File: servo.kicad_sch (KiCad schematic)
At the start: 13 parts, among them J301 pow, M301 Motor_Servo, Q301 BC547, SW301 switch, SW302 switch, U301 LM555xN

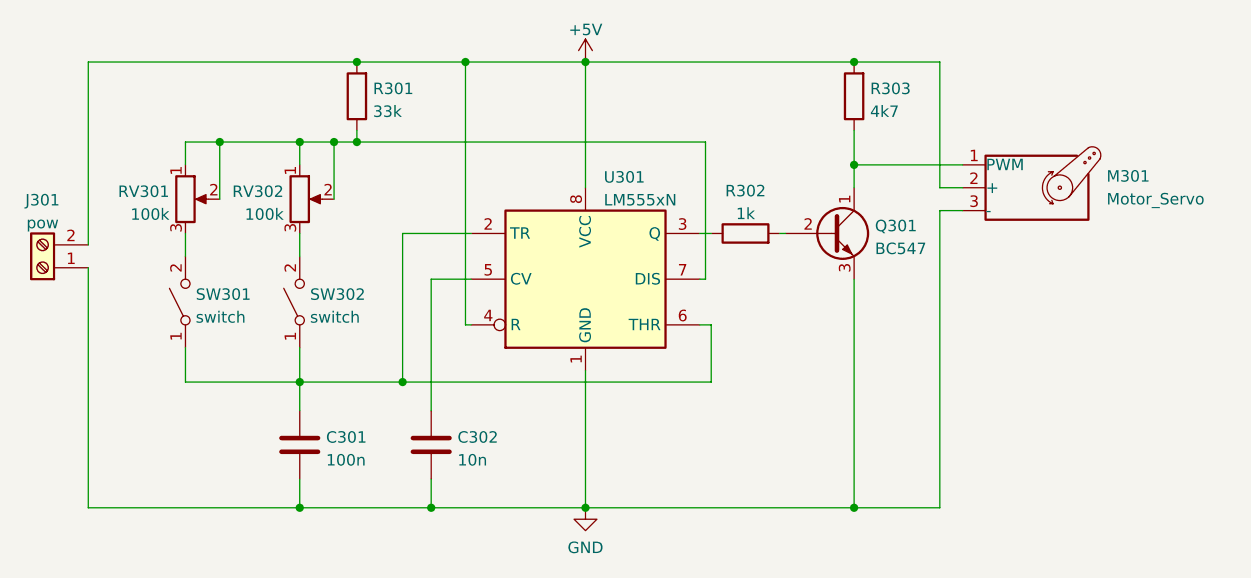
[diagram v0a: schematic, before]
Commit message: added hierarchial labels to some schematics
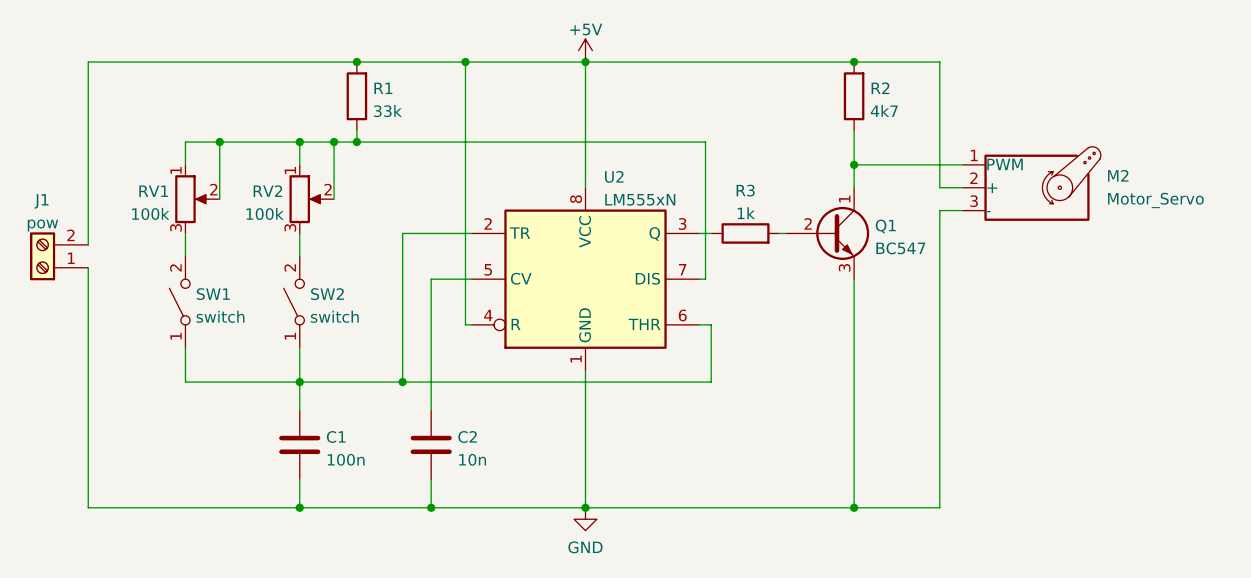
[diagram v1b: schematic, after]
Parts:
- renumbered C301 to C1, C302 to C2, J301 to J1, M301 to M2, Q301 to Q1, R301 to R1, R303 to R2, R302 to R3, RV301 to RV1, RV302 to RV2, SW301 to SW1, SW302 to SW2, U301 to U2

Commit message: moved some schematic scheets to their own folders and routed a board with it. This allow for re-use of PCB parts.
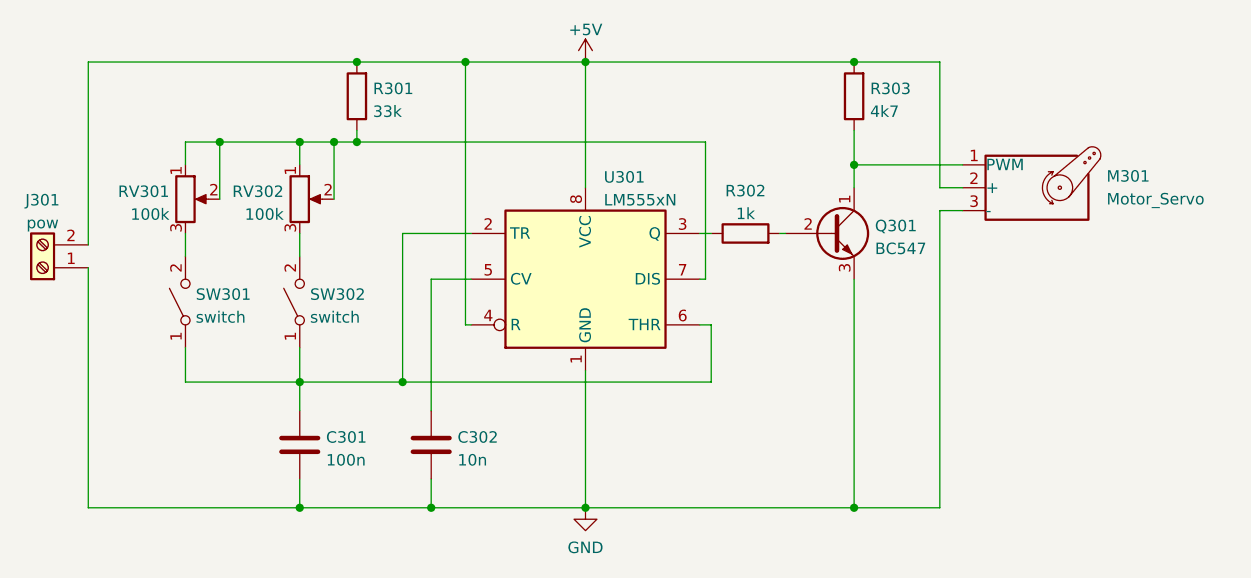
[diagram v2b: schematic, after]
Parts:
- renumbered C1 to C301, C2 to C302, J1 to J301, M2 to M301, Q1 to Q301, R1 to R301, R3 to R302, R2 to R303, RV1 to RV301, RV2 to RV302, SW1 to SW301, SW2 to SW302, U2 to U301
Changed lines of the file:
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@@
   (symbol (lib_id "Device:R_Potentiometer") (at 127 78.74 0) (unit 1)
     (in_bom yes) (on_board yes) (dnp no) (fields_autoplaced)
-    (property "Reference" "RV2" (at 125.2221 77.9053 0)
+    (property "Reference" "RV302" (at 125.2221 77.9053 0)
       (effects (font (size 1.27 1.27)) (justify right))
     )
@@
       (project "general_schematics"
         (path "/e777d9ec-d073-4229-a9e6-2cf85636e407/c8788370-a7f5-4096-b7be-5f9bdb412f73"
-          (reference "RV2") (unit 1)
+          (reference "RV302") (unit 1)
         )
       )
@@
   (symbol (lib_id "Device:R") (at 176.53 82.55 90) (unit 1)
     (in_bom yes) (on_board yes) (dnp no) (fields_autoplaced)
-    (property "Reference" "R3" (at 176.53 77.8342 90)
+    (property "Reference" "R302" (at 176.53 77.8342 90)
       (effects (font (size 1.27 1.27)))
     )
@@
       (project "general_schematics"
         (path "/e777d9ec-d073-4229-a9e6-2cf85636e407/c8788370-a7f5-4096-b7be-5f9bdb412f73"
-          (reference "R3") (unit 1)
+          (reference "R302") (unit 1)
         )
       )
@@
   (symbol (lib_id "Device:C") (at 141.605 106.045 0) (unit 1)
     (in_bom yes) (on_board yes) (dnp no) (fields_autoplaced)
-    (property "Reference" "C2" (at 144.526 105.2103 0)
+    (property "Reference" "C302" (at 144.526 105.2103 0)
       (effects (font (size 1.27 1.27)) (justify left))
     )
@@
       (project "general_schematics"
         (path "/e777d9ec-d073-4229-a9e6-2cf85636e407/c8788370-a7f5-4096-b7be-5f9bdb412f73"
-          (reference "C2") (unit 1)
+          (reference "C302") (unit 1)
         )
       )
@@
   (symbol (lib_id "Device:C") (at 127 106.045 0) (unit 1)
     (in_bom yes) (on_board yes) (dnp no) (fields_autoplaced)
-    (property "Reference" "C1" (at 129.921 105.2103 0)
+    (property "Reference" "C301" (at 129.921 105.2103 0)
       (effects (font (size 1.27 1.27)) (justify left))
     )
@@
       (project "general_schematics"
         (path "/e777d9ec-d073-4229-a9e6-2cf85636e407/c8788370-a7f5-4096-b7be-5f9bdb412f73"
-          (reference "C1") (unit 1)
+          (reference "C301") (unit 1)
         )
       )
@@
   (symbol (lib_id "power:GND") (at 158.75 113.03 0) (unit 1)
     (in_bom yes) (on_board yes) (dnp no) (fields_autoplaced)
-    (property "Reference" "#PWR04" (at 158.75 119.38 0)
+    (property "Reference" "#PWR0103" (at 158.75 119.38 0)
       (effects (font (size 1.27 1.27)) hide)
     )
@@
       (project "general_schematics"
         (path "/e777d9ec-d073-4229-a9e6-2cf85636e407/c8788370-a7f5-4096-b7be-5f9bdb412f73"
-          (reference "#PWR04") (unit 1)
+          (reference "#PWR0103") (unit 1)
         )
       )
@@
   (symbol (lib_id "Device:R_Potentiometer") (at 114.3 78.74 0) (unit 1)
     (in_bom yes) (on_board yes) (dnp no) (fields_autoplaced)
-    (property "Reference" "RV1" (at 112.5221 77.9053 0)
+    (property "Reference" "RV301" (at 112.5221 77.9053 0)
       (effects (font (size 1.27 1.27)) (justify right))
     )
@@
       (project "general_schematics"
         (path "/e777d9ec-d073-4229-a9e6-2cf85636e407/c8788370-a7f5-4096-b7be-5f9bdb412f73"
-          (reference "RV1") (unit 1)
+          (reference "RV301") (unit 1)
         )
       )
@@
   (symbol (lib_id "Switch:SW_SPST") (at 127 90.17 90) (unit 1)
     (in_bom yes) (on_board yes) (dnp no) (fields_autoplaced)
-    (property "Reference" "SW2" (at 128.143 89.3353 90)
+    (property "Reference" "SW302" (at 128.143 89.3353 90)
       (effects (font (size 1.27 1.27)) (justify right))
     )
@@
       (project "general_schematics"
         (path "/e777d9ec-d073-4229-a9e6-2cf85636e407/c8788370-a7f5-4096-b7be-5f9bdb412f73"
-          (reference "SW2") (unit 1)
+          (reference "SW302") (unit 1)
         )
       )
@@
   (symbol (lib_id "Connector:Screw_Terminal_01x02") (at 98.425 86.36 180) (unit 1)
     (in_bom yes) (on_board yes) (dnp no) (fields_autoplaced)
-    (property "Reference" "J1" (at 98.425 78.8502 0)
+    (property "Reference" "J301" (at 98.425 78.8502 0)
       (effects (font (size 1.27 1.27)))
     )
@@
       (project "general_schematics"
         (path "/e777d9ec-d073-4229-a9e6-2cf85636e407/c8788370-a7f5-4096-b7be-5f9bdb412f73"
-          (reference "J1") (unit 1)
+          (reference "J301") (unit 1)
         )
       )
@@
   (symbol (lib_id "Switch:SW_SPST") (at 114.3 90.17 90) (unit 1)
     (in_bom yes) (on_board yes) (dnp no) (fields_autoplaced)
-    (property "Reference" "SW1" (at 115.443 89.3353 90)
+    (property "Reference" "SW301" (at 115.443 89.3353 90)
       (effects (font (size 1.27 1.27)) (justify right))
     )
@@
       (project "general_schematics"
         (path "/e777d9ec-d073-4229-a9e6-2cf85636e407/c8788370-a7f5-4096-b7be-5f9bdb412f73"
-          (reference "SW1") (unit 1)
+          (reference "SW301") (unit 1)
         )
       )
@@
   (symbol (lib_id "Device:R") (at 188.595 67.31 180) (unit 1)
     (in_bom yes) (on_board yes) (dnp no) (fields_autoplaced)
-    (property "Reference" "R2" (at 190.373 66.4753 0)
+    (property "Reference" "R303" (at 190.373 66.4753 0)
       (effects (font (size 1.27 1.27)) (justify right))
     )
@@
       (project "general_schematics"
         (path "/e777d9ec-d073-4229-a9e6-2cf85636e407/c8788370-a7f5-4096-b7be-5f9bdb412f73"
-          (reference "R2") (unit 1)
+          (reference "R303") (unit 1)
         )
       )
@@
   (symbol (lib_id "Device:R") (at 133.35 67.31 180) (unit 1)
     (in_bom yes) (on_board yes) (dnp no) (fields_autoplaced)
-    (property "Reference" "R1" (at 135.128 66.4753 0)
+    (property "Reference" "R301" (at 135.128 66.4753 0)
       (effects (font (size 1.27 1.27)) (justify right))
     )
@@
       (project "general_schematics"
         (path "/e777d9ec-d073-4229-a9e6-2cf85636e407/c8788370-a7f5-4096-b7be-5f9bdb412f73"
-          (reference "R1") (unit 1)
+          (reference "R301") (unit 1)
         )
       )
@@
   (symbol (lib_id "Transistor_BJT:BC547") (at 186.055 82.55 0) (unit 1)
     (in_bom yes) (on_board yes) (dnp no) (fields_autoplaced)
-    (property "Reference" "Q1" (at 190.9064 81.7153 0)
+    (property "Reference" "Q301" (at 190.9064 81.7153 0)
       (effects (font (size 1.27 1.27)) (justify left))
     )
@@
       (project "general_schematics"
         (path "/e777d9ec-d073-4229-a9e6-2cf85636e407/c8788370-a7f5-4096-b7be-5f9bdb412f73"
-          (reference "Q1") (unit 1)
+          (reference "Q301") (unit 1)
         )
       )
@@
   (symbol (lib_id "power:+5V") (at 158.75 63.5 0) (unit 1)
     (in_bom yes) (on_board yes) (dnp no) (fields_autoplaced)
-    (property "Reference" "#PWR03" (at 158.75 67.31 0)
+    (property "Reference" "#PWR0104" (at 158.75 67.31 0)
       (effects (font (size 1.27 1.27)) hide)
     )
@@
       (project "general_schematics"
         (path "/e777d9ec-d073-4229-a9e6-2cf85636e407/c8788370-a7f5-4096-b7be-5f9bdb412f73"
-          (reference "#PWR03") (unit 1)
+          (reference "#PWR0104") (unit 1)
         )
       )
@@
   (symbol (lib_id "Timer:LM555xN") (at 158.75 87.63 0) (unit 1)
     (in_bom yes) (on_board yes) (dnp no) (fields_autoplaced)
-    (property "Reference" "U2" (at 160.7694 76.3102 0)
+    (property "Reference" "U301" (at 160.7694 76.3102 0)
       (effects (font (size 1.27 1.27)) (justify left))
     )
@@
       (project "general_schematics"
         (path "/e777d9ec-d073-4229-a9e6-2cf85636e407/c8788370-a7f5-4096-b7be-5f9bdb412f73"
-          (reference "U2") (unit 1)
+          (reference "U301") (unit 1)
         )
       )
@@
   (symbol (lib_id "Motor:Motor_Servo") (at 208.28 77.47 0) (unit 1)
     (in_bom yes) (on_board yes) (dnp no) (fields_autoplaced)
-    (property "Reference" "M2" (at 216.6398 76.2019 0)
+    (property "Reference" "M301" (at 216.6398 76.2019 0)
       (effects (font (size 1.27 1.27)) (justify left))
     )
@@
       (project "general_schematics"
         (path "/e777d9ec-d073-4229-a9e6-2cf85636e407/c8788370-a7f5-4096-b7be-5f9bdb412f73"
-          (reference "M2") (unit 1)
-        )
-      )
+          (reference "M301") (unit 1)
+        )
+      )
